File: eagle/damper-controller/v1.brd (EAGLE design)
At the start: 39.4 x 41.9 mm, 18 parts, among them IC1 ULN2003AD, Q1 RS485-ADAPTER0.05-CONNECTOR

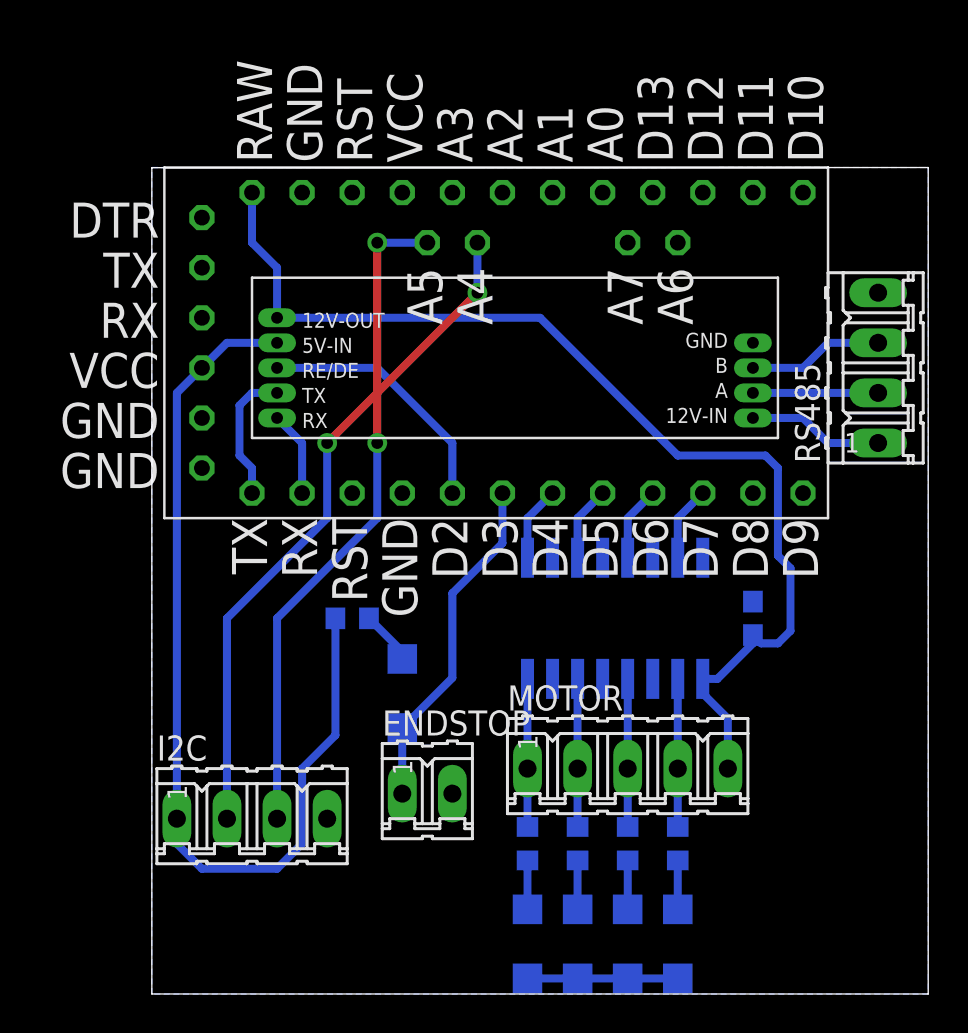
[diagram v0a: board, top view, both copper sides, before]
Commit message: Finished damper controller, and modified for OSH Park print, instead of home-made method
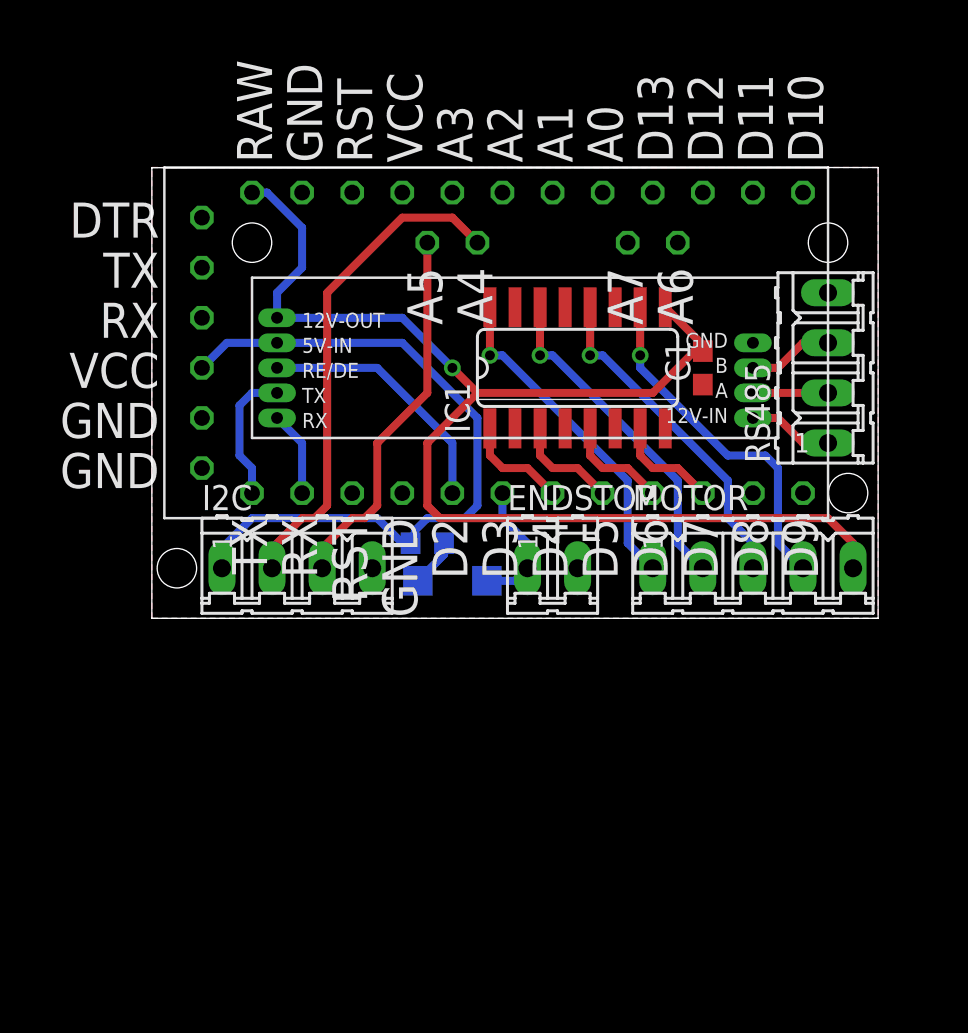
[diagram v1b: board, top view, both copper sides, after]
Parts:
- removed LED1, LED2, LED3, LED4: (no value), led:SML1206
- removed R1, R2, R3, R4: 2k2, resistor:R0603
- R5: value 1k -> 10k
- moved ENDSTOP 13.1 mm to (21.6, 21.6)
- moved C1 13.0 mm to (29.2, 31.8), flipped to the top, turned to 270 degrees
- moved I2C 12.9 mm to (8.64, 21.6)
- moved IC1 12.8 mm to (22.9, 31.8), flipped to the top, turned to 0 degrees
- moved MOTOR 12.0 mm to (31.8, 21.6)
- moved LED5 6.25 mm to (16.5, 21.0), turned to 0 degrees
- moved R5 5.39 mm to (15.2, 22.9)
- moved RS485 2.54 mm to (35.6, 31.8)
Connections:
- removed net N$6: LED4.A, R4.1
- removed net N$7: LED3.A, R3.1
- removed net N$8: LED2.A, R2.1
- removed net N$9: LED1.A, R1.1
- net GND: no longer LED1.C, LED2.C, LED3.C, LED4.C
- net N$2: no longer R1.2
- net N$3: no longer R2.2
- net N$4: no longer R3.2
- net N$5: no longer R4.2
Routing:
- net SLC: track 33.9 -> 19.1 mm, vias 2 -> 0
- net VCC: track 48.5 -> 36.7 mm
- net +12V: track 55.1 -> 65.8 mm, vias 0 -> 1
- net N$12: track 17.3 -> 6.66 mm
- net N$5: track 7.51 -> 17.8 mm, vias 0 -> 1
- net N$3: track 7.51 -> 17.0 mm, vias 0 -> 1
- net N$2: track 7.51 -> 17.0 mm, vias 0 -> 1
- net N$4: track 7.51 -> 17.0 mm, vias 0 -> 1
- net SDA: track 34.5 -> 25.2 mm, vias 2 -> 0
- net GND: track 7.62 -> 0.00 mm
- net N$10: track 6.35 -> 3.81 mm
- net N$11: track 6.88 -> 4.34 mm
- net N$1: track 6.88 -> 4.34 mm
- net N$9: track 2.48 -> 0.00 mm
- net N$8: track 2.48 -> 0.00 mm
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- added copper zone on layer 1, net GND
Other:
- board size 39.4 x 41.9 mm -> 36.8 x 22.9 mm

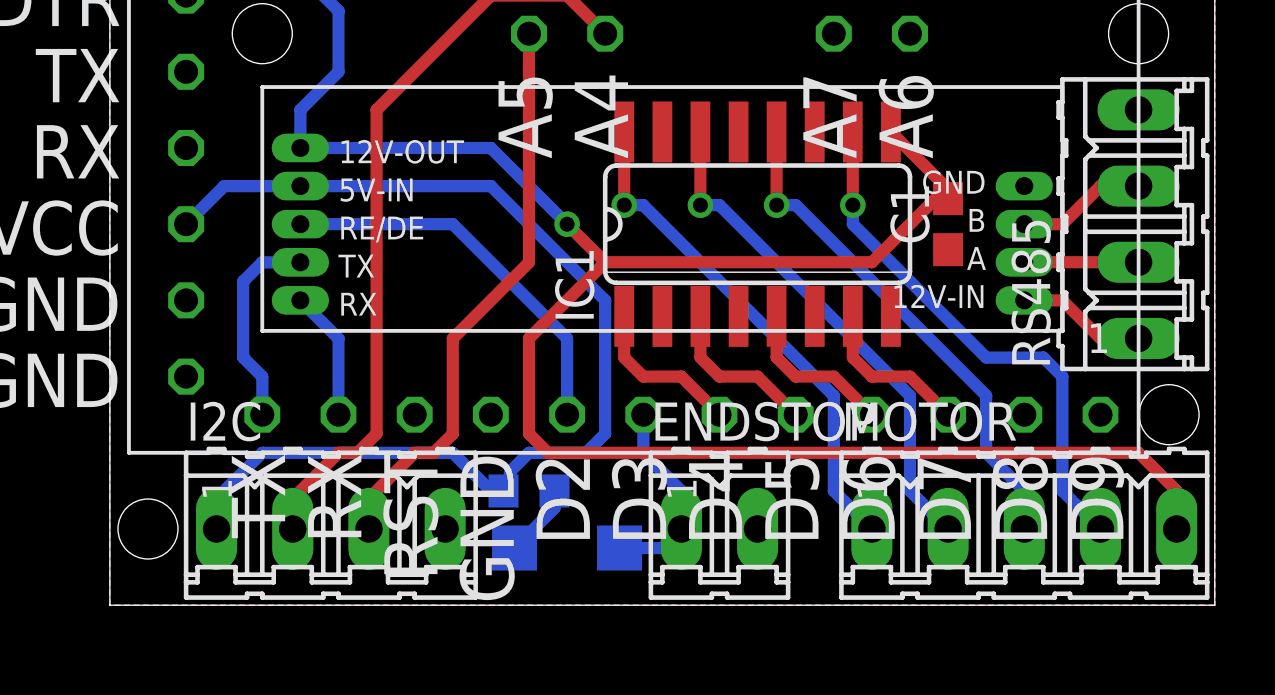
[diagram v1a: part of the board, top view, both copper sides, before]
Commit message: Adjusting damper controller board based on first prototype of PCB. Needed to move switch connector, and removed LED, as there is no space.
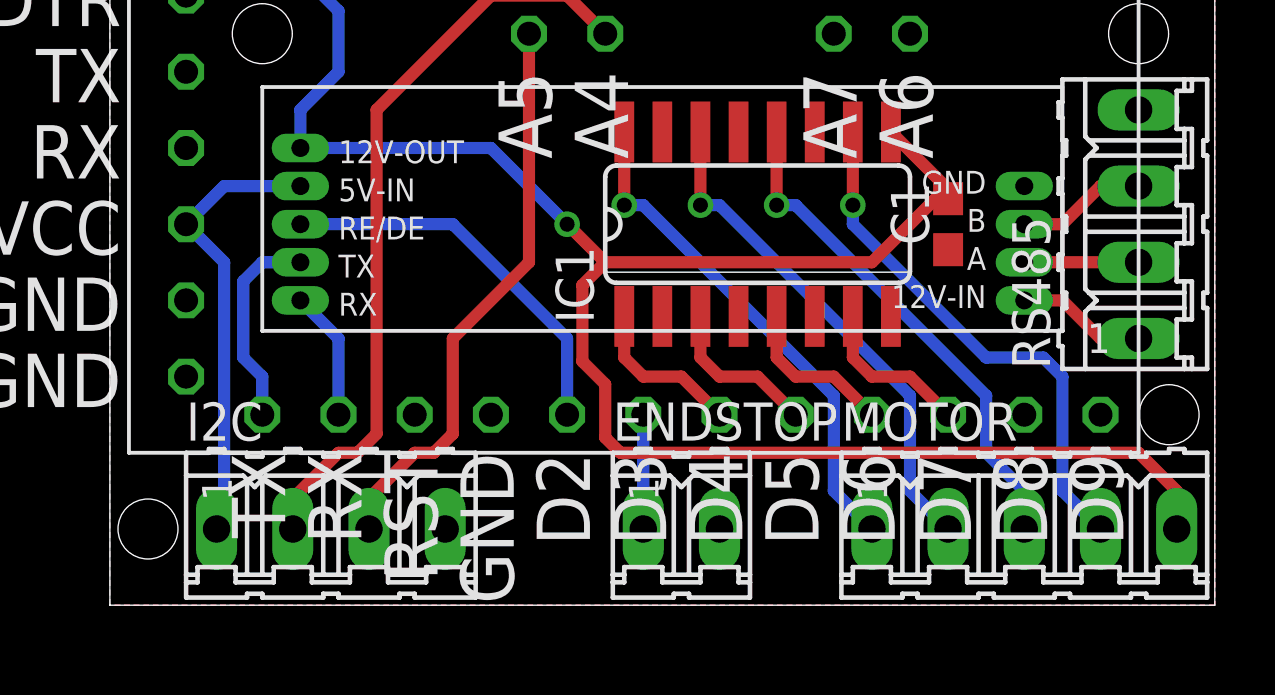
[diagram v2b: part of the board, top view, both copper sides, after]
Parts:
- removed LED5: (no value), led:SML1206
- removed R5: 10k, resistor:R0603
- moved ENDSTOP 1.27 mm to (20.3, 21.6)
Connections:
- removed net N$13: LED5.A, R5.2
- net N$12: no longer LED5.C
- net VCC: no longer R5.1
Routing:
- net VCC: track 36.7 -> 15.1 mm
- net +12V: track 65.8 -> 63.0 mm
- net N$12: track 6.66 -> 3.81 mm
- net N$13: track 2.46 -> 0.00 mm
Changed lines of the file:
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@@
 <attribute name="MF" value="" x="31.75" y="21.59" size="1.778" layer="27" display="off"/>
 </element>
-<element name="ENDSTOP" library="con-amp-quick" package="02P" value="" x="21.59" y="21.59">
-<attribute name="MPN" value="" x="21.59" y="21.59" size="1.778" layer="27" display="off"/>
-<attribute name="OC_NEWARK" value="unknown" x="21.59" y="21.59" size="1.778" layer="27" display="off"/>
-<attribute name="OC_FARNELL" value="unknown" x="21.59" y="21.59" size="1.778" layer="27" display="off"/>
-<attribute name="MF" value="" x="21.59" y="21.59" size="1.778" layer="27" display="off"/>
+<element name="ENDSTOP" library="con-amp-quick" package="02P" value="" x="20.32" y="21.59">
+<attribute name="MPN" value="" x="20.32" y="21.59" size="1.778" layer="27" display="off"/>
+<attribute name="OC_NEWARK" value="unknown" x="20.32" y="21.59" size="1.778" layer="27" display="off"/>
+<attribute name="OC_FARNELL" value="unknown" x="20.32" y="21.59" size="1.778" layer="27" display="off"/>
+<attribute name="MF" value="" x="20.32" y="21.59" size="1.778" layer="27" display="off"/>
 </element>
 <element name="C1" library="eagle-ltspice" package="C0603" value="" x="29.21" y="31.75" smashed="yes" rot="R270">
@@
 <attribute name="VALUE" x="27.305" y="32.385" size="1.27" layer="27" rot="R270"/>
 </element>
-<element name="LED5" library="led" package="SML1206" value="" x="16.51" y="20.955" rot="MR0"/>
-<element name="R5" library="resistor" package="R0603" value="10k" x="15.24" y="22.86" rot="MR180"/>
 <element name="I2C" library="con-amp-quick" package="04P" value="" x="8.636" y="21.59">
 <attribute name="MPN" value="" x="8.636" y="21.59" size="1.778" layer="27" display="off"/>
@@
 <contactref element="U$1" pad="VCC1"/>
 <contactref element="Q1" pad="5V-IN"/>
-<contactref element="R5" pad="1"/>
 <wire x1="7.62" y1="33.02" x2="5.08" y2="33.02" width="0.4064" layer="16"/>
 <wire x1="5.08" y1="33.02" x2="3.81" y2="31.75" width="0.4064" layer="16"/>
 <contactref element="I2C" pad="1"/>
-<wire x1="4.826" y1="21.59" x2="4.826" y2="22.606" width="0.4064" layer="16"/>
-<wire x1="4.826" y1="22.606" x2="6.35" y2="24.13" width="0.4064" layer="16"/>
-<wire x1="6.35" y1="24.13" x2="12.7" y2="24.13" width="0.4064" layer="16"/>
-<wire x1="12.7" y1="24.13" x2="13.97" y2="22.86" width="0.4064" layer="16"/>
-<wire x1="13.97" y1="22.86" x2="14.39" y2="22.86" width="0.4064" layer="16"/>
-<wire x1="7.62" y1="33.02" x2="13.97" y2="33.02" width="0.4064" layer="16"/>
-<wire x1="13.97" y1="33.02" x2="17.78" y2="29.21" width="0.4064" layer="16"/>
-<wire x1="17.78" y1="29.21" x2="17.78" y2="24.765" width="0.4064" layer="16"/>
-<wire x1="17.78" y1="24.765" x2="17.145" y2="24.13" width="0.4064" layer="16"/>
-<wire x1="17.145" y1="24.13" x2="15.24" y2="24.13" width="0.4064" layer="16"/>
-<wire x1="15.24" y1="24.13" x2="14.605" y2="23.495" width="0.4064" layer="16"/>
-<wire x1="14.605" y1="23.495" x2="14.605" y2="23.075" width="0.4064" layer="16"/>
-<wire x1="14.605" y1="23.075" x2="14.39" y2="22.86" width="0.4064" layer="16"/>
-<wire x1="13.97" y1="33.02" x2="13.97" y2="40.64" width="0" layer="19" extent="16-16"/>
+<wire x1="4.826" y1="21.59" x2="5.08" y2="21.844" width="0.4064" layer="16"/>
+<wire x1="5.08" y1="21.844" x2="5.08" y2="30.48" width="0.4064" layer="16"/>
+<wire x1="5.08" y1="30.48" x2="3.81" y2="31.75" width="0.4064" layer="16"/>
+<wire x1="7.62" y1="33.02" x2="13.97" y2="40.64" width="0" layer="19" extent="1-1"/>
 </signal>
 <signal name="+12V">
@@
 <wire x1="36.83" y1="21.59" x2="36.83" y2="22.86" width="0.4064" layer="1"/>
 <wire x1="36.83" y1="22.86" x2="35.56" y2="24.13" width="0.4064" layer="1"/>
-<wire x1="35.56" y1="24.13" x2="15.875" y2="24.13" width="0.4064" layer="1"/>
-<wire x1="15.875" y1="24.13" x2="15.24" y2="24.765" width="0.4064" layer="1"/>
-<wire x1="15.24" y1="24.765" x2="15.24" y2="27.94" width="0.4064" layer="1"/>
-<wire x1="15.24" y1="27.94" x2="17.78" y2="30.48" width="0.4064" layer="1"/>
+<wire x1="35.56" y1="24.13" x2="18.288" y2="24.13" width="0.4064" layer="1"/>
+<wire x1="17.018" y1="29.718" x2="17.78" y2="30.48" width="0.4064" layer="1"/>
 <wire x1="7.62" y1="34.29" x2="7.62" y2="35.56" width="0.4064" layer="16"/>
 <wire x1="7.62" y1="35.56" x2="8.89" y2="36.83" width="0.4064" layer="16"/>
@@
 <wire x1="8.89" y1="38.862" x2="7.112" y2="40.64" width="0.4064" layer="16"/>
 <wire x1="7.112" y1="40.64" x2="6.35" y2="40.64" width="0.4064" layer="16"/>
+<wire x1="18.288" y1="24.13" x2="17.78" y2="24.638" width="0.4064" layer="1"/>
+<wire x1="17.78" y1="24.638" x2="17.78" y2="26.416" width="0.4064" layer="1"/>
+<wire x1="17.78" y1="26.416" x2="17.018" y2="27.178" width="0.4064" layer="1"/>
+<wire x1="17.018" y1="27.178" x2="17.018" y2="29.718" width="0.4064" layer="1"/>
 </signal>
 <signal name="N$2">
@@
 <contactref element="ENDSTOP" pad="1"/>
 <contactref element="U$1" pad="D3"/>
-<contactref element="LED5" pad="C"/>
-<wire x1="18.26" y1="20.955" x2="19.685" y2="20.955" width="0.4064" layer="16"/>
-<wire x1="19.685" y1="20.955" x2="20.32" y2="21.59" width="0.4064" layer="16"/>
-<wire x1="20.32" y1="21.59" x2="20.32" y2="22.86" width="0.4064" layer="16"/>
-<wire x1="20.32" y1="22.86" x2="19.05" y2="24.13" width="0.4064" layer="16"/>
-<wire x1="19.05" y1="24.13" x2="19.05" y2="25.4" width="0.4064" layer="16"/>
-</signal>
-<signal name="N$13">
-<contactref element="R5" pad="2"/>
-<contactref element="LED5" pad="A"/>
-<wire x1="16.09" y1="22.86" x2="16.09" y2="22.285" width="0.4064" layer="16"/>
-<wire x1="16.09" y1="22.285" x2="14.76" y2="20.955" width="0.4064" layer="16"/>
+<wire x1="19.05" y1="25.4" x2="19.05" y2="21.59" width="0.4064" layer="16"/>
 </signal>
 <signal name="SDA">
